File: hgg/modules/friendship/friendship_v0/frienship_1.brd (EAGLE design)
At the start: 100 x 80 mm, 31 parts, among them IC5 741G66DBV, IC6 741G66DBV, IC7 741G66DBV, IC8 741G66DBV

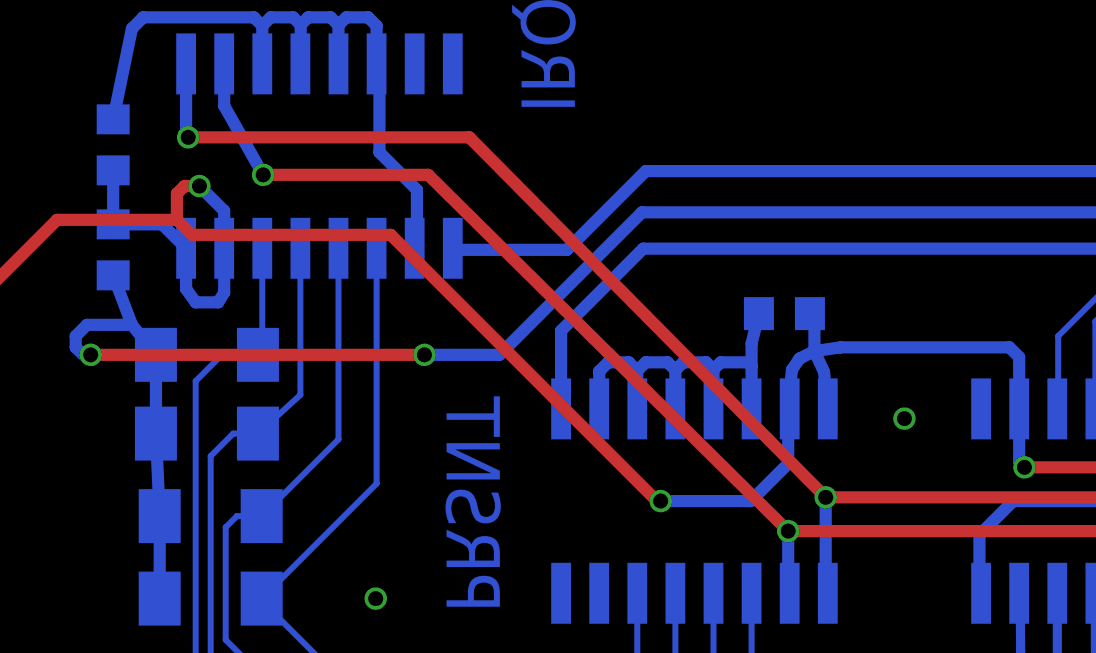
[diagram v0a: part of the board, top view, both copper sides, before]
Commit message: fixed a bug: shift enable must be defaulted to low
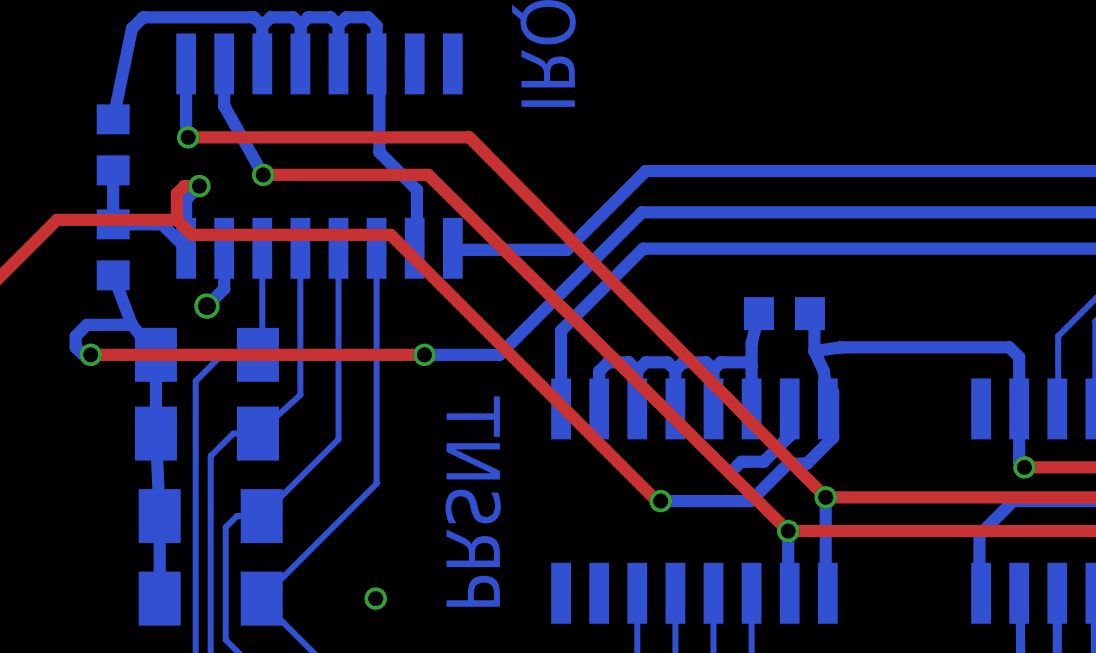
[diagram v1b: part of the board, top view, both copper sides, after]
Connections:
- net 3V3: no longer IRQ_LATCH.15, PRSNT_LATCH.15
- net GND: now also IRQ_LATCH.15, PRSNT_LATCH.15
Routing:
- net GND: track 589.5 -> 594.9 mm
- net 3V3: track 243.0 -> 237.6 mm
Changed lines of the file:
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@@
 <layer number="18" name="Vias" color="2" fill="1" visible="yes" active="yes"/>
 <layer number="19" name="Unrouted" color="6" fill="1" visible="yes" active="yes"/>
-<layer number="20" name="Dimension" color="15" fill="1" visible="no" active="yes"/>
-<layer number="21" name="tPlace" color="7" fill="1" visible="no" active="yes"/>
-<layer number="22" name="bPlace" color="7" fill="1" visible="no" active="yes"/>
+<layer number="20" name="Dimension" color="15" fill="1" visible="yes" active="yes"/>
+<layer number="21" name="tPlace" color="7" fill="1" visible="yes" active="yes"/>
+<layer number="22" name="bPlace" color="7" fill="1" visible="yes" active="yes"/>
 <layer number="23" name="tOrigins" color="15" fill="1" visible="yes" active="yes"/>
 <layer number="24" name="bOrigins" color="15" fill="1" visible="yes" active="yes"/>
-<layer number="25" name="tNames" color="7" fill="1" visible="no" active="yes"/>
-<layer number="26" name="bNames" color="7" fill="1" visible="no" active="yes"/>
-<layer number="27" name="tValues" color="7" fill="1" visible="no" active="yes"/>
-<layer number="28" name="bValues" color="7" fill="1" visible="no" active="yes"/>
+<layer number="25" name="tNames" color="7" fill="1" visible="yes" active="yes"/>
+<layer number="26" name="bNames" color="7" fill="1" visible="yes" active="yes"/>
+<layer number="27" name="tValues" color="7" fill="1" visible="yes" active="yes"/>
+<layer number="28" name="bValues" color="7" fill="1" visible="yes" active="yes"/>
 <layer number="29" name="tStop" color="7" fill="3" visible="yes" active="yes"/>
 <layer number="30" name="bStop" color="7" fill="6" visible="yes" active="yes"/>
@@
 Covered vias can be set in Masks (Limit).
 &lt;/p&gt;Your Beta LAYOUT Team</description>
+<description language="en">&lt;b&gt;EAGLE Design Rules&lt;/b&gt;
+&lt;p&gt;
+The default Design Rules have been set to cover
+a wide range of applications. Your particular design
+may have different requirements, so please make the
+necessary adjustments and save your customized
+design rules under a new name.
+</description>
 <param name="layerSetup" value="(1*16)"/>
 <param name="mtCopper" value="0.035mm 0.035mm 0.035mm 0.035mm 0.035mm 0.035mm 0.035mm 0.035mm 0.035mm 0.035mm 0.035mm 0.035mm 0.035mm 0.035mm 0.035mm 0.035mm"/>
@@
 <via x="13.625" y="21.75" extent="1-16" drill="0.5"/>
 <via x="15.75" y="21.75" extent="1-16" drill="0.5"/>
-<via x="46.375" y="57.875" extent="1-16" drill="0.5"/>
 <via x="89" y="34.5" extent="1-16" drill="0.5"/>
 <via x="87.625" y="17" extent="1-16" drill="0.5"/>
@@
 <via x="76" y="17" extent="1-16" drill="0.5"/>
 <via x="36" y="17" extent="1-16" drill="0.5"/>
+<contactref element="PRSNT_LATCH" pad="15"/>
+<contactref element="IRQ_LATCH" pad="15"/>
+<wire x1="42.55" y1="58.1984" x2="42.55" y2="57.3" width="0.4064" layer="16"/>
+<wire x1="42.55" y1="57.3" x2="41.6875" y2="56.4375" width="0.4064" layer="16"/>
+<wire x1="41.6875" y1="56.4375" x2="40.9375" y2="56.4375" width="0.4064" layer="16"/>
+<wire x1="40.9375" y1="56.4375" x2="40.75" y2="56.25" width="0.4064" layer="16"/>
+<wire x1="23.7" y1="63.5516" x2="23.7" y2="62.2" width="0.4064" layer="16"/>
+<wire x1="23.7" y1="62.2" x2="23.125" y2="61.625" width="0.4064" layer="16"/>
+<via x="23.125" y="61.625" extent="1-16" drill="0.6"/>
+<wire x1="23.125" y1="61.625" x2="22.9375" y2="61.625" width="0.4064" layer="1"/>
 </signal>
 <signal name="TX-">
@@
 <contactref element="R7" pad="2"/>
 <contactref element="R12" pad="2"/>
-<contactref element="PRSNT_LATCH" pad="15"/>
-<contactref element="IRQ_LATCH" pad="15"/>
 <contactref element="INTACK_LATCH" pad="10"/>
 <contactref element="R5" pad="2"/>
@@
 <wire x1="20" y1="64.35" x2="21.6316" y2="64.35" width="0.4064" layer="16"/>
 <wire x1="21.6316" y1="64.35" x2="22.43" y2="63.5516" width="0.4064" layer="16"/>
-<wire x1="22.43" y1="63.5516" x2="22.43" y2="62.195" width="0.4064" layer="16"/>
-<wire x1="22.43" y1="62.195" x2="22.75" y2="61.75" width="0.4064" layer="16"/>
-<wire x1="22.75" y1="61.75" x2="23.5" y2="61.75" width="0.4064" layer="16"/>
-<wire x1="23.5" y1="61.75" x2="23.7" y2="62.075" width="0.4064" layer="16"/>
-<wire x1="23.7" y1="62.075" x2="23.7" y2="63.5516" width="0.4064" layer="16"/>
-<wire x1="43.82" y1="58.1984" x2="43.695" y2="59.43" width="0.4064" layer="16"/>
+<wire x1="43.82" y1="58.1984" x2="43.735665625" y2="59.029328125" width="0.4064" layer="16"/>
+<wire x1="43.735665625" y1="59.029328125" x2="43.695" y2="59.43" width="0.4064" layer="16"/>
 <wire x1="43.695" y1="59.43" x2="43.375" y2="60.125" width="0.4064" layer="16"/>
-<wire x1="43.375" y1="60.125" x2="42.875" y2="59.875" width="0.4064" layer="16"/>
-<wire x1="42.875" y1="59.875" x2="42.625" y2="59.5" width="0.4064" layer="16"/>
-<wire x1="42.625" y1="59.5" x2="42.5" y2="58.25" width="0.4064" layer="16"/>
-<wire x1="42.5" y1="58.25" x2="42.625" y2="58.125" width="0.125" layer="16"/>
-<wire x1="42.625" y1="58.125" x2="42.5" y2="58.125" width="0.125" layer="16"/>
 <wire x1="43.225" y1="61.375" x2="43.375" y2="61.225" width="0.125" layer="16"/>
 <wire x1="43.375" y1="61.225" x2="43.375" y2="60.125" width="0.4064" layer="16"/>
-<wire x1="23.7" y1="63.5516" x2="23.7" y2="64.8" width="0.4064" layer="16"/>
-<wire x1="23.7" y1="64.8" x2="22.875" y2="65.625" width="0.4064" layer="16"/>
 <via x="22.875" y="65.625" extent="1-16" drill="0.5"/>
 <wire x1="22.875" y1="65.625" x2="22.375" y2="65.625" width="0.4064" layer="1"/>
@@
 <wire x1="38.25" y1="55.125" x2="41.25" y2="55.125" width="0.4064" layer="16"/>
 <wire x1="41.25" y1="55.125" x2="42.5" y2="56.375" width="0.4064" layer="16"/>
-<wire x1="42.5" y1="56.375" x2="42.5" y2="58.125" width="0.4064" layer="16"/>
-<wire x1="42.5" y1="58.25" x2="42.5" y2="58.125" width="0.4064" layer="16"/>
-<wire x1="42.55" y1="58.1984" x2="42.55" y2="58.175" width="0.4064" layer="16"/>
-<wire x1="42.55" y1="58.175" x2="42.5" y2="58.125" width="0.4064" layer="16"/>
 <wire x1="50.2" y1="58.1984" x2="50.2" y2="59.925" width="0.4064" layer="16"/>
 <wire x1="50.2" y1="59.925" x2="49.875" y2="60.25" width="0.4064" layer="16"/>
@@
 <wire x1="16" y1="32.625" x2="16.625" y2="32" width="0.4064" layer="1"/>
 <wire x1="16.625" y1="32" x2="18" y2="32" width="0.4064" layer="1"/>
+<wire x1="22.43" y1="63.5516" x2="22.43" y2="65.18" width="0.4064" layer="16"/>
+<wire x1="22.43" y1="65.18" x2="22.875" y2="65.625" width="0.4064" layer="16"/>
+<wire x1="42.5" y1="56.375" x2="43.125" y2="56.375" width="0.4064" layer="16"/>
+<wire x1="43.125" y1="56.375" x2="44" y2="57.25" width="0.4064" layer="16"/>
+<wire x1="44" y1="57.25" x2="44" y2="58.76499375" width="0.4064" layer="16"/>
+<wire x1="44" y1="58.76499375" x2="43.735665625" y2="59.029328125" width="0.4064" layer="16"/>
 </signal>
 <signal name="5V">

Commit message: added pullups to IRQ lines
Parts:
- added R14, R15, R16, R17: 10k, rcl:R0603
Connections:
- net 3V3: now also R14.2, R15.2, R16.2, R17.2
- net IRQ0: now also R17.1
- net IRQ1: now also R16.1
- net IRQ2: now also R15.1
- net IRQ3: now also R14.1
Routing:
- net 3V3: track 237.6 -> 246.6 mm
- net IRQ2: track 65.6 -> 69.0 mm
- net IRQ3: track 84.3 -> 87.6 mm
- net IRQ1: track 44.8 -> 48.0 mm
- net IRQ0: track 30.0 -> 32.9 mm
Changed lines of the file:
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@@
 <element name="R11" library="rcl" package="R0603" value="120" x="12.75" y="8" rot="MR0"/>
 <element name="R13" library="rcl" package="R0603" value="120" x="88.25" y="7.25" rot="MR270"/>
+<element name="R14" library="rcl" package="R0603" value="10k" x="87.8125" y="35.125" rot="R270"/>
+<element name="R15" library="rcl" package="R0603" value="10k" x="67.835246875" y="35.050475" rot="R270"/>
+<element name="R16" library="rcl" package="R0603" value="10k" x="47.625" y="35" rot="R270"/>
+<element name="R17" library="rcl" package="R0603" value="10k" x="27.4375" y="35.1875" rot="R270"/>
 </elements>
 <signals>
@@
 <via x="13.625" y="21.75" extent="1-16" drill="0.5"/>
 <via x="15.75" y="21.75" extent="1-16" drill="0.5"/>
-<via x="89" y="34.5" extent="1-16" drill="0.5"/>
+<via x="90.375" y="34.6875" extent="1-16" drill="0.5"/>
 <via x="87.625" y="17" extent="1-16" drill="0.5"/>
 <via x="86" y="2.375" extent="1-16" drill="0.5"/>
@@
 <wire x1="22.75" y1="40.125" x2="24.5" y2="38.375" width="0.2" layer="16"/>
 <wire x1="24.5" y1="38.375" x2="24.5" y2="36" width="0.2" layer="16"/>
+<contactref element="R17" pad="1"/>
+<wire x1="24.5" y1="36" x2="27.4" y2="36" width="0.4064" layer="1"/>
+<wire x1="27.4" y1="36" x2="27.4375" y2="36.0375" width="0.4064" layer="1"/>
 </signal>
 <signal name="/CS0">
@@
 <wire x1="43.125" y1="39" x2="44.5" y2="37.625" width="0.2" layer="16"/>
 <wire x1="44.5" y1="37.625" x2="44.5" y2="36" width="0.2" layer="16"/>
+<contactref element="R16" pad="1"/>
+<wire x1="44.5" y1="36" x2="47.475" y2="36" width="0.4064" layer="1"/>
+<wire x1="47.475" y1="36" x2="47.625" y2="35.85" width="0.4064" layer="1"/>
 </signal>
 <signal name="/CS1">
 <contactref element="PORT1" pad="A03(/CS,IRQ)"/>
 <contactref element="INTACK_LATCH" pad="6"/>
-<wire x1="46.25" y1="36" x2="46.25" y2="45.5" width="0.3048" layer="1"/>
-<wire x1="47.125" y1="46.375" x2="50.75" y2="46.375" width="0.3048" layer="1"/>
-<wire x1="50.75" y1="46.375" x2="51.5" y2="47.125" width="0.3048" layer="1"/>
+<wire x1="49.625" y1="36" x2="49.625" y2="45.3125" width="0.3048" layer="1"/>
 <wire x1="51.5" y1="47.125" x2="51.47" y2="48.095" width="0.3048" layer="1"/>
 <wire x1="51.47" y1="48.095" x2="51.47" y2="52.0516" width="0.3048" layer="16"/>
 <via x="51.47" y="48.095" extent="1-16" drill="0.5"/>
-<wire x1="42.5" y1="35" x2="45.375" y2="35" width="0.3048" layer="1"/>
-<wire x1="45.375" y1="35" x2="46.25" y2="36" width="0.3048" layer="1"/>
-<wire x1="47.125" y1="46.375" x2="46.25" y2="45.5" width="0.3048" layer="1"/>
+<wire x1="42.5" y1="35" x2="48.75" y2="35" width="0.3048" layer="1"/>
+<wire x1="48.75" y1="35" x2="49.625" y2="36" width="0.3048" layer="1"/>
+<wire x1="51.5" y1="47.125" x2="49.625" y2="45.3125" width="0.3048" layer="1"/>
 </signal>
 <signal name="IRQ2">
@@
 <wire x1="35.625" y1="43" x2="31.25" y2="43" width="0.2" layer="16"/>
 <wire x1="31.25" y1="43" x2="23.75" y2="50.5" width="0.2" layer="16"/>
+<contactref element="R15" pad="1"/>
+<wire x1="64.5" y1="36" x2="67.735721875" y2="36" width="0.4064" layer="1"/>
+<wire x1="67.735721875" y1="36" x2="67.835246875" y2="35.900475" width="0.4064" layer="1"/>
 </signal>
 <signal name="/CS2">
@@
 <wire x1="25.125" y1="51.75" x2="25" y2="51.75" width="0.3048" layer="16"/>
 <wire x1="25" y1="51.75" x2="24.75" y2="52" width="0.3048" layer="16"/>
+<contactref element="R14" pad="1"/>
+<wire x1="84.5" y1="36" x2="87.7875" y2="36" width="0.4064" layer="1"/>
+<wire x1="87.7875" y1="36" x2="87.8125" y2="35.975" width="0.4064" layer="1"/>
 <wire x1="25" y1="51.875" x2="24.95" y2="51.875" width="0" layer="19" extent="16-16"/>
 </signal>
@@
 <wire x1="72.5" y1="32" x2="73.375" y2="32.4" width="0.4064" layer="16"/>
 <wire x1="93.238" y1="34.125" x2="91.113" y2="32" width="0.4064" layer="1"/>
-<wire x1="91.113" y1="32" x2="84.5" y2="32" width="0.4064" layer="1"/>
+<wire x1="91.113" y1="32" x2="87.9375" y2="32" width="0.4064" layer="1"/>
+<wire x1="87.9375" y1="32" x2="84.5" y2="32" width="0.4064" layer="1"/>
 <wire x1="18" y1="32" x2="12.5" y2="31.9" width="0.4064" layer="16"/>
 <contactref element="IC5" pad="5"/>
@@
 <wire x1="44" y1="57.25" x2="44" y2="58.76499375" width="0.4064" layer="16"/>
 <wire x1="44" y1="58.76499375" x2="43.735665625" y2="59.029328125" width="0.4064" layer="16"/>
+<contactref element="R14" pad="2"/>
+<contactref element="R15" pad="2"/>
+<contactref element="R16" pad="2"/>
+<contactref element="R17" pad="2"/>
+<wire x1="27.4375" y1="34.3375" x2="27.4375" y2="32.0625" width="0.4064" layer="1"/>
+<wire x1="27.4375" y1="32.0625" x2="27.5" y2="32" width="0.4064" layer="1"/>
+<wire x1="47.625" y1="34.15" x2="47.625" y2="32" width="0.4064" layer="1"/>
+<wire x1="67.835246875" y1="34.200475" x2="67.835246875" y2="32.039753125" width="0.4064" layer="1"/>
+<wire x1="67.835246875" y1="32.039753125" x2="67.875" y2="32" width="0.4064" layer="1"/>
+<wire x1="87.8125" y1="34.275" x2="87.8125" y2="32.125" width="0.4064" layer="1"/>
+<wire x1="87.8125" y1="32.125" x2="87.9375" y2="32" width="0.4064" layer="1"/>
 </signal>
 <signal name="5V">

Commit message: moved diodes next to PCIe connector, rerouting, IRQ pullups now on bottom
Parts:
- moved D1 65.5 mm to (87.8, 40.6), turned to 90 degrees
- moved D4 46.7 mm to (67.8, 40.6), turned to 90 degrees
- moved D2 29.6 mm to (47.6, 40.7), turned to 90 degrees
- moved D3 20.1 mm to (28.7, 40.7), turned to 90 degrees
- moved R17 0.20 mm to (27.5, 35.0), flipped to the bottom
- flipped R14 to the bottom
- flipped R15 to the bottom
- flipped R16 to the bottom
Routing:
- net N$11: track 74.2 -> 165.1 mm, vias 2 -> 3
- net 3V3: track 246.6 -> 234.1 mm, vias 10 -> 11
- net /CS0: track 37.8 -> 48.1 mm
- net IRQ3: track 87.6 -> 93.7 mm
- net GND: track 594.9 -> 599.1 mm, vias 32 -> 33
- net IRQ1: track 48.0 -> 50.9 mm
- net IRQ0: track 32.9 -> 34.7 mm
- net PRSNT2: track 54.3 -> 55.8 mm
- net PRSNT3: track 74.1 -> 75.4 mm
- net IRQ2: track 69.0 -> 70.2 mm, vias 3 -> 4
- net /CS1: track 24.4 -> 25.3 mm
- net /CS3: track 43.7 -> 44.5 mm, vias 1 -> 2

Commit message: using new busmaster plug, more ground vias
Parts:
- removed BUSMASTER: (no value), pinhead:2X05
- added U$1: BUSMASTER_PLUG, hgg:BUSMASTER_SLOT
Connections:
- new net N$12: U$1.A11(GND)
- net GND: no longer BUSMASTER.6
- net N$1: now also U$1.A13(INTACK_SER); no longer BUSMASTER.3
- net N$11: now also U$1.A03(IRQ); no longer BUSMASTER.9
- net N$13: now also U$1.A05(PRSNT_DATAIN); no longer BUSMASTER.8
- net N$17: now also U$1.A01(IRQ_DATAIN); no longer BUSMASTER.10
- net N$3: now also U$1.A15(SH/LD_PRSNT/IRQ); no longer BUSMASTER.1
- net N$4: now also U$1.A07(INTACK_SCK); no longer BUSMASTER.7
- net N$9: now also U$1.A09(INTACK_RCK); no longer BUSMASTER.5
- net SHIFT: now also U$1.A17(IRQ/PRSNT_CLK); no longer BUSMASTER.2
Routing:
- net GND: track 599.1 -> 579.7 mm, vias 33 -> 124
- net SHIFT: track 61.0 -> 72.7 mm
- net N$17: track 44.1 -> 54.1 mm
- net N$13: track 43.0 -> 52.9 mm
- net N$11: track 165.1 -> 174.0 mm
- net N$3: track 66.6 -> 74.4 mm
- net N$1: track 24.0 -> 31.6 mm
- net N$4: track 28.9 -> 35.8 mm
- net N$9: track 27.8 -> 33.4 mm
- net N$6: track 34.8 -> 34.0 mm
- net TDI: track 89.8 -> 89.0 mm
- net N$7: track 36.5 -> 35.8 mm
- net N$2: track 33.7 -> 33.0 mm
- net IRQ3: track 93.7 -> 93.0 mm

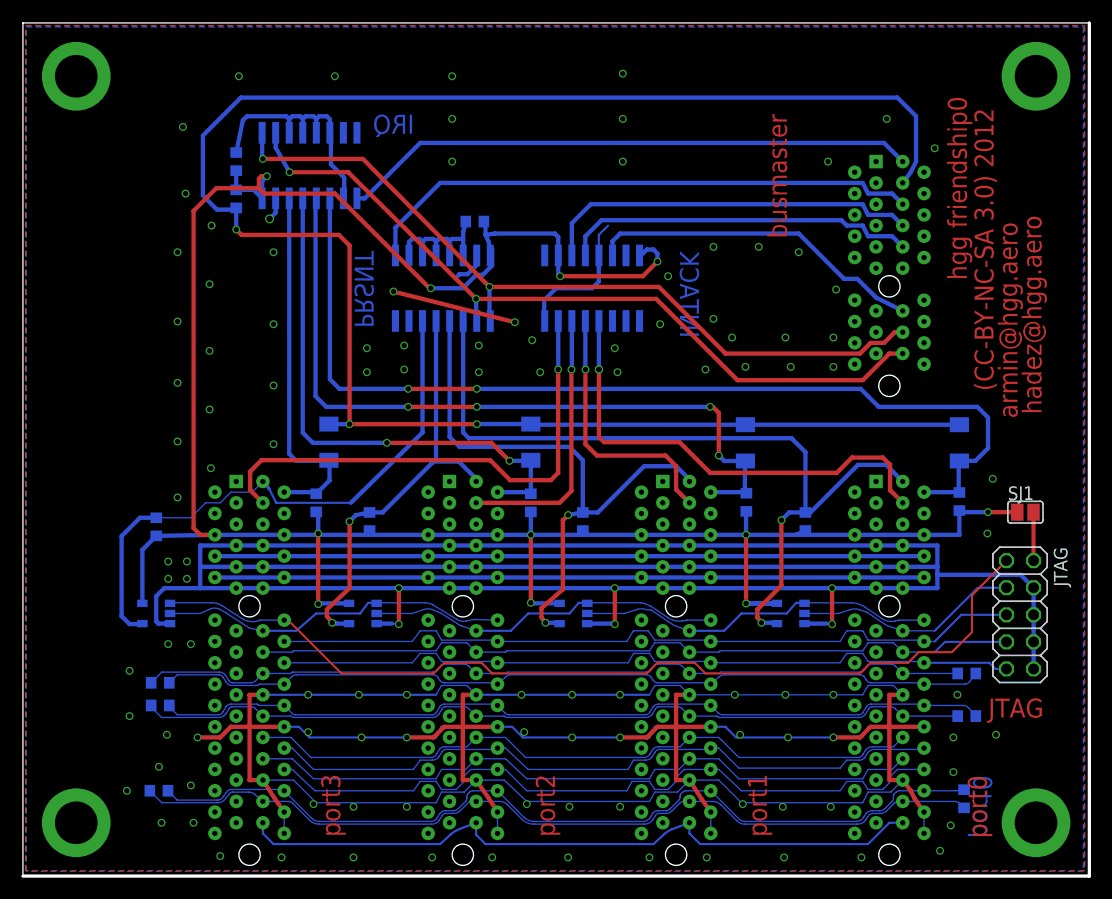
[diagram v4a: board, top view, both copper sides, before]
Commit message: increased resttring from 0 to 25%. fixed DRC issues
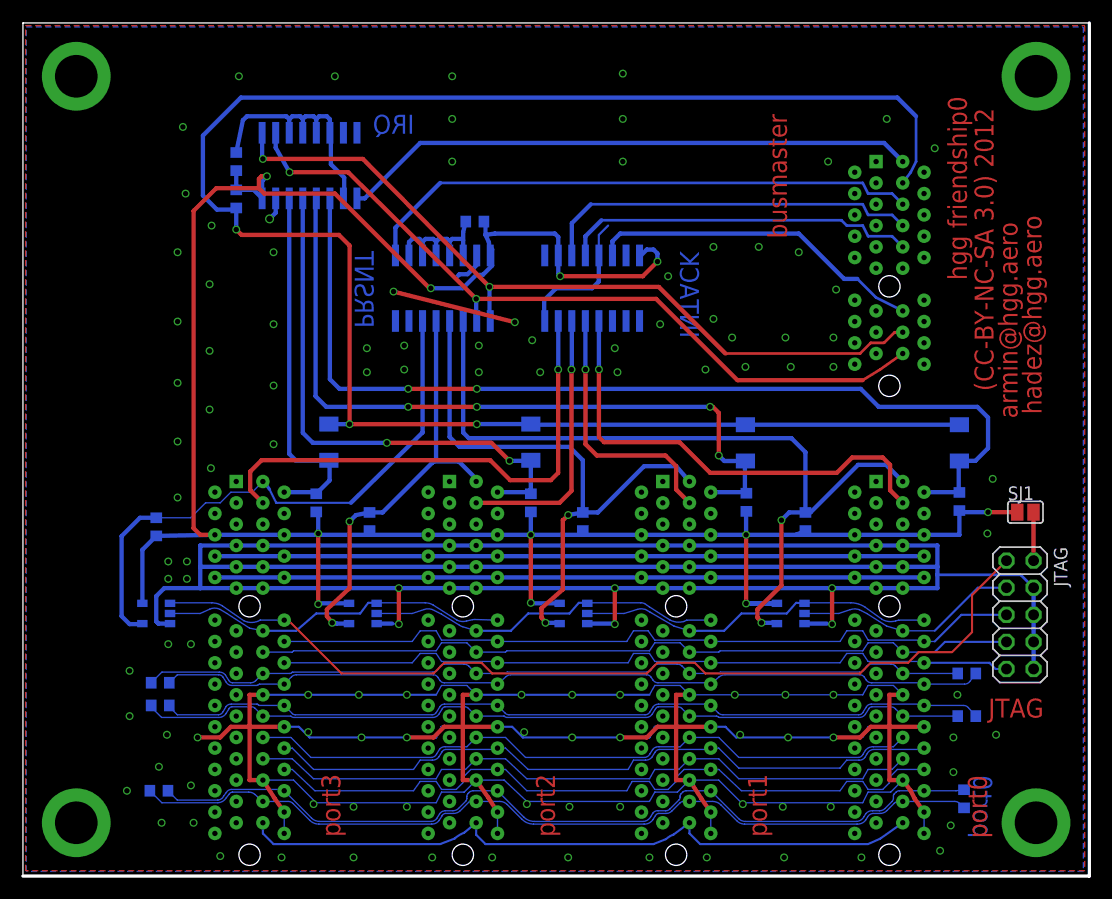
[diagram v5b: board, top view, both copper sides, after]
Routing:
- net IRQ1: track 50.9 -> 52.7 mm
- net /CS3: vias 2 -> 1
